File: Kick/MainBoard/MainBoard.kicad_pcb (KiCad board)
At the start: 4 copper layers, 128.8 x 67 mm, 15 parts, among them J1 CN1 / J11, J2 CN2 / J12, J3 Conn_02x15_Odd_Even, J4 Conn_02x10_Odd_Even, J5 Conn_02x15_Odd_Even, J6 Conn_02x10_Odd_Even, U2 NX3L4053, U3 NX3L4053, U4 MIC5504-1.8YM5

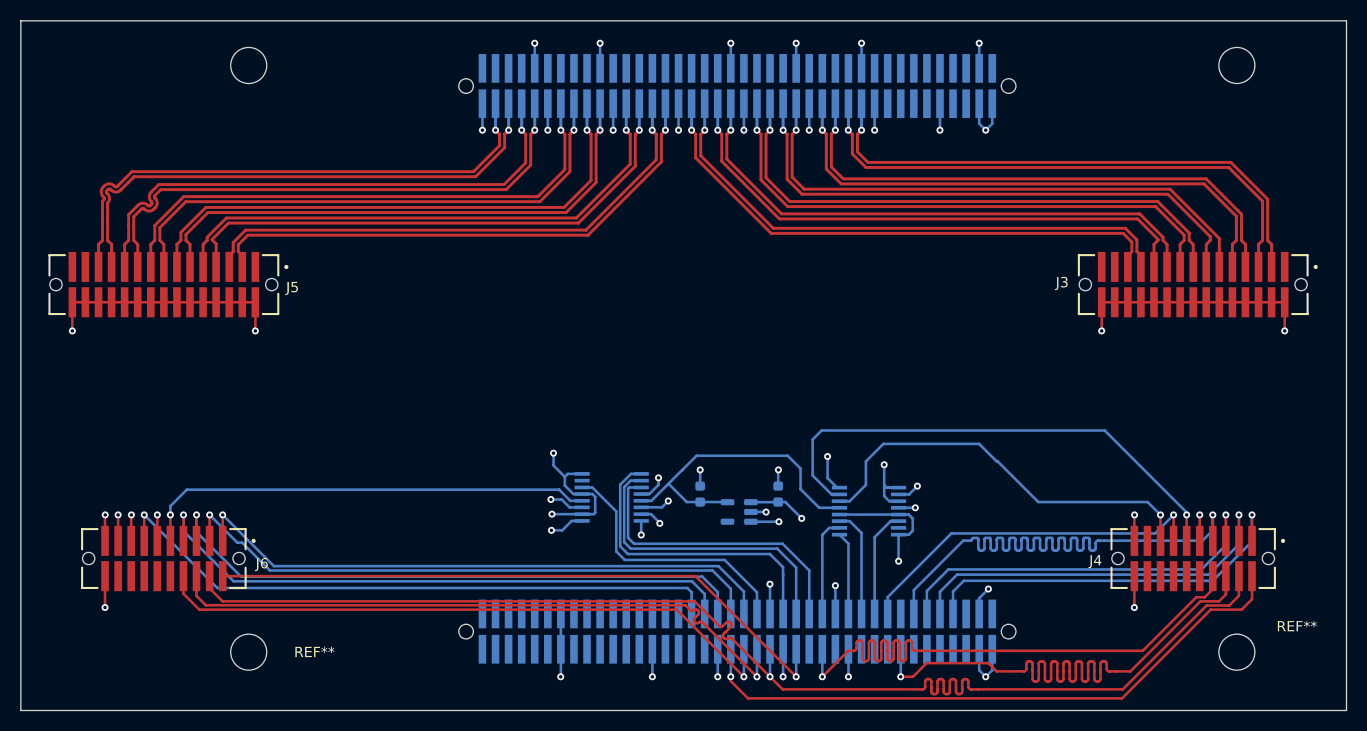
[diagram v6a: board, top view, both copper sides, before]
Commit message: new design and PCB with available clock pins and LED pins. Still cross-domain timing issues.
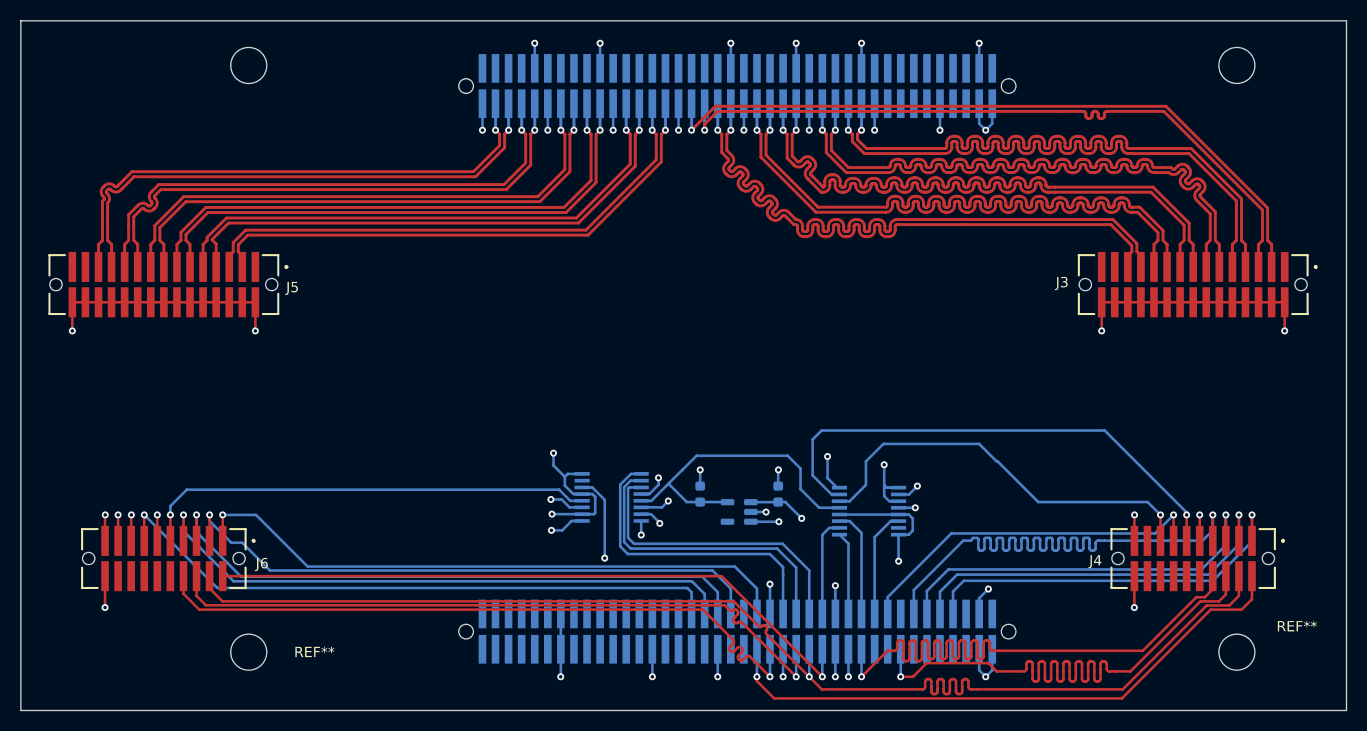
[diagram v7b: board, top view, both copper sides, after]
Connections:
- J1 pad 22: unconnected-(J1-Pin_22-Pad22) -> /ss_0
- J1 pad 26: unconnected-(J1-Pin_26-Pad26) -> /sw_~{E}_1
- J1 pad 28: /ss_0 -> /sck
- J1 pad 30: unconnected-(J1-Pin_30-Pad30) -> /miso
- J1 pad 32: /sck -> /mosi
- J1 pad 36: /miso -> /ss_1
- J1 pad 37: /sw_~{E}_1 -> /monitor1_1
- J1 pad 38: /mosi -> /sck
- J1 pad 39: /monitor1_1 -> unconnected-(J1-Pin_39-Pad39)
- J1 pad 40: /ss_1 -> unconnected-(J1-Pin_40-Pad40)
- J1 pad 42: /sck -> unconnected-(J1-Pin_42-Pad42)
- J2 pad 22: /clkout0_N -> /dout0_0_N
- J2 pad 24: /clkout0_P -> /dout0_0_P
- J2 pad 26: /dout0_0_N -> /dout1_0_N
- J2 pad 28: /dout0_0_P -> /dout1_0_P
- J2 pad 32: /dout1_0_N -> /dout2_0_N
- J2 pad 34: /dout1_0_P -> /dout2_0_P
- J2 pad 36: /dout2_0_N -> /dout3_0_N
- J2 pad 38: /dout2_0_P -> /dout3_0_P
- J2 pad 42: /dout3_0_N -> /sync0_N
- J2 pad 44: /dout3_0_P -> /sync0_P
- J2 pad 46: /sync0_N -> /clkout0_P
- J2 pad 48: /sync0_P -> /clkout0_N
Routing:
- net /sw_~{E}_1: track 25.6 -> 42.2 mm, vias 0 -> 2
- net /clkout0_N: track 53.3 -> 69.5 mm
- net /clkout0_P: track 53.4 -> 69.4 mm
- net /dout3_0_P: track 54.1 -> 65.6 mm
- net /dout3_0_N: track 54.1 -> 65.6 mm
- net /dout0_0_P: track 53.3 -> 64.8 mm
- net /dout0_0_N: track 53.3 -> 64.8 mm
- net /sync0_P: track 53.8 -> 65.1 mm
- net /sync0_N: track 53.8 -> 65.1 mm
- net /dout2_0_P: track 54.2 -> 64.6 mm
- net /dout2_0_N: track 54.2 -> 64.6 mm
- net /dout1_0_N: track 54.0 -> 64.4 mm
- net /dout1_0_P: track 54.0 -> 64.4 mm
- net /ss_1: track 62.2 -> 67.6 mm
- net /ss_0: track 61.1 -> 66.0 mm
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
